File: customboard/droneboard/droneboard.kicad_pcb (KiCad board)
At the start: 4 copper layers, 38 x 38 mm, 49 parts, among them J1 Conn_01x04, J3 Conn_01x05_Pin, J4 Conn_01x02_Pin, J7 Conn_01x04_Odd_Even, SW1 SW_Push, SW2 SW_Push, U1 STM32F411CEUx, U3 L78M05CDT, U4 ICM-42688-P, U5 LDK130M33R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

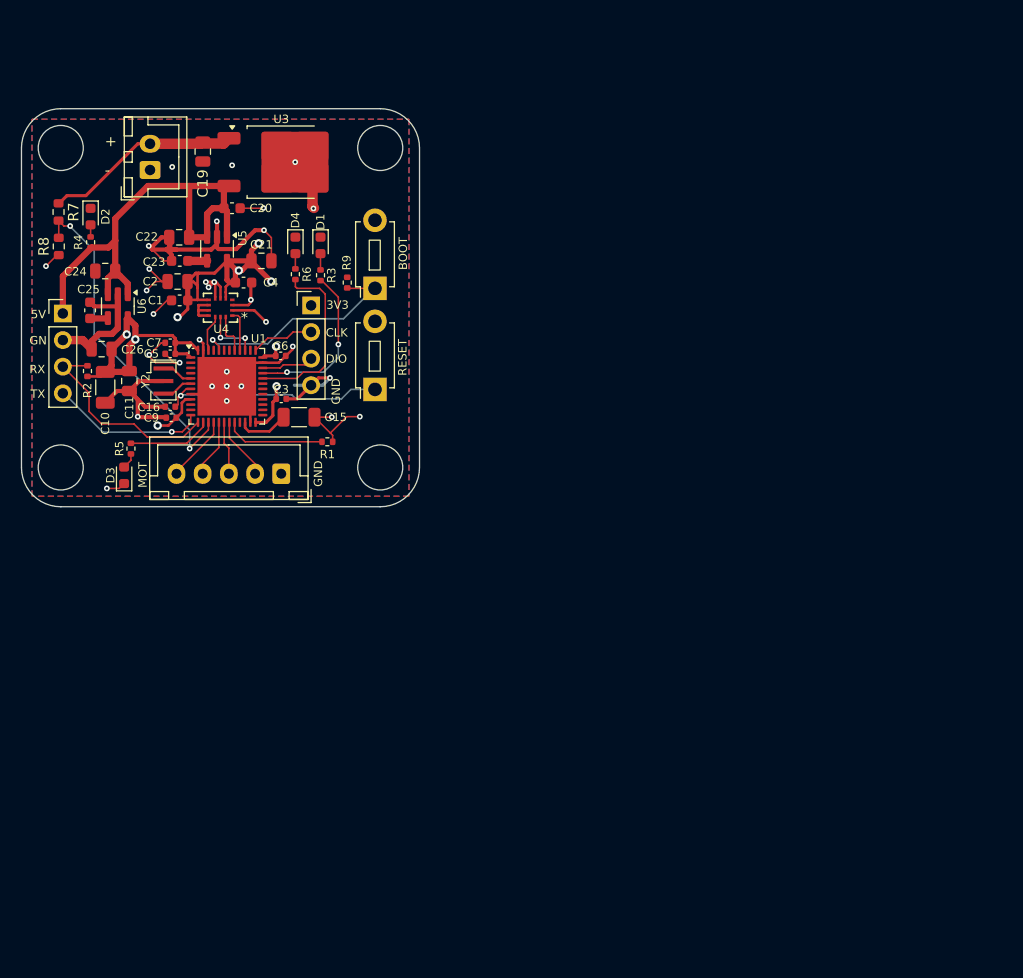
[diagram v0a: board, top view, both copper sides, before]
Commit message: stm32f7 initial work
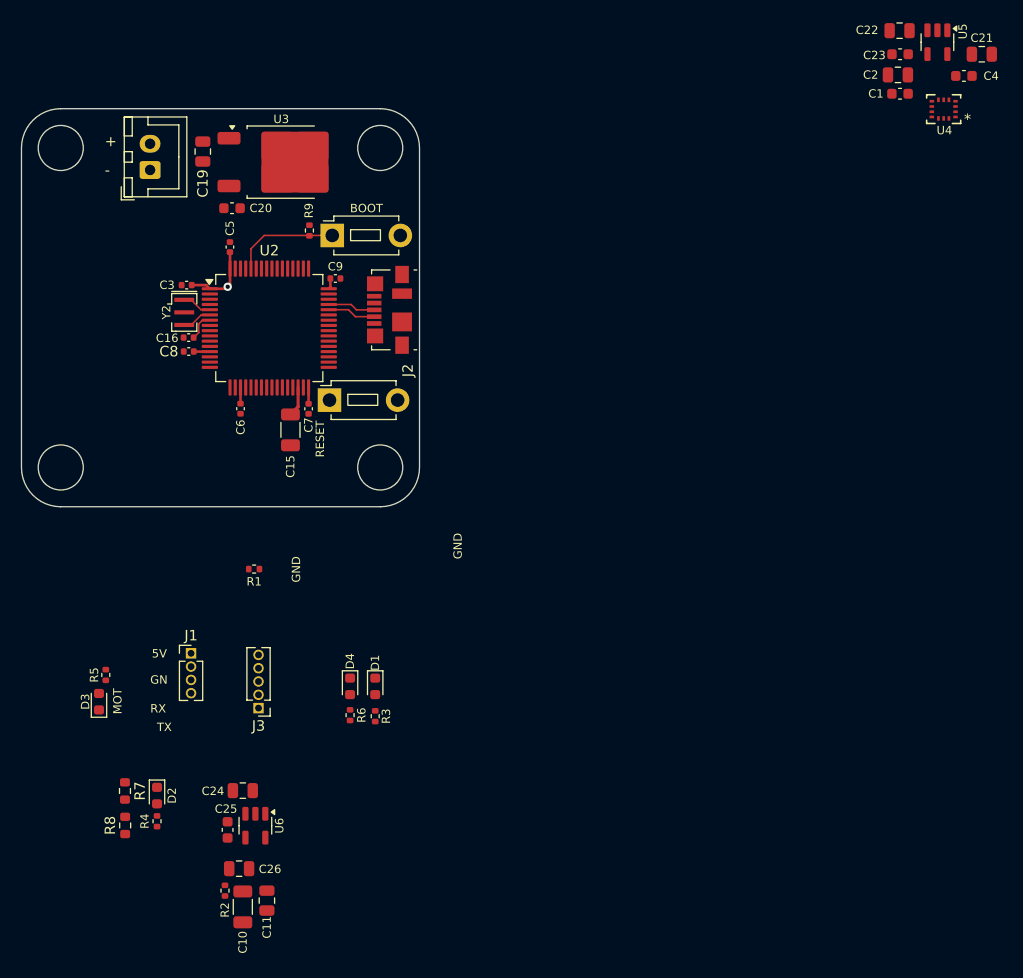
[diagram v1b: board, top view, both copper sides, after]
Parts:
- removed J7: Conn_01x04_Odd_Even, Connector_PinHeader_2.54mm:PinHeader_1x04_P2.54mm_Vertical
- removed U1: STM32F411CEUx, Package_DFN_QFN:QFN-48-1EP_7x7mm_P0.5mm_EP5.6x5.6mm
- added C8: 100n, Capacitor_SMD:C_0402_1005Metric, F.Cu at (66.0, 105.2)
- added J2: USB_B_Micro, Connector_USB:USB_Micro-B_Molex_47346-0001, F.Cu at (85.1, 101.2)
- added U2: STM32F722RETx, Package_QFP:LQFP-64_10x10mm_P0.5mm, F.Cu at (73.7, 102.9)
- J1: footprint Connector_PinHeader_2.54mm:PinHeader_1x04_P2.54mm_Vertical -> Connector_PinHeader_1.27mm:PinHeader_1x04_P1.27mm_Vertical
- J3: footprint Connector_JST:JST_XH_B5B-XH-A_1x05_P2.50mm_Vertical -> Connector_PinHeader_1.27mm:PinHeader_1x05_P1.27mm_Vertical
- moved U4 71.6 mm to (138.0, 82.0)
- moved C1 71.5 mm to (133.9, 80.6)
- moved C2 71.5 mm to (133.7, 78.8)
- moved C21 71.5 mm to (141.7, 76.8)
- moved C22 71.5 mm to (133.8, 74.5)
- moved C23 71.5 mm to (133.9, 76.8)
- moved U5 71.5 mm to (137.4, 75.6)
- moved C4 71.5 mm to (140.0, 78.9)
- moved R4 55.6 mm to (62.9, 150.0)
- moved R8 55.6 mm to (59.9, 150.4)
- moved D2 55.6 mm to (62.9, 147.6)
- moved R7 55.6 mm to (59.9, 147.1)
- moved C26 51.3 mm to (70.8, 154.6)
- moved R2 51.3 mm to (69.4, 156.7)
- moved C10 51.3 mm to (71.1, 158.2)
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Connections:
- R1 pad 1: Net-(U1-PB2) -> unconnected-(R1-Pad1)
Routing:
- net /GND: track 134.7 -> 0.00 mm, vias 31 -> 0
- net /5V: track 48.2 -> 0.00 mm
- net /VBATMON: track 32.2 -> 0.00 mm, vias 2 -> 0
- net /VGYRO: track 30.2 -> 0.00 mm, vias 4 -> 0
- net /VMCU: track 36.8 -> 12.8 mm, vias 5 -> 1
- net /RX3: track 20.0 -> 0.00 mm
- net /RESET1: track 21.9 -> 2.71 mm, vias 1 -> 0
- net /12V: track 18.9 -> 0.00 mm
- net /BLUE: track 17.1 -> 0.00 mm
- net /YELLOW: track 16.0 -> 0.00 mm, vias 2 -> 0
- net /TX3: track 14.9 -> 0.00 mm, vias 1 -> 0
- net /BOOT: track 21.8 -> 10.2 mm, vias 1 -> 0
- net Net-(U1-PB2): track 9.62 -> 0.00 mm
- net /GREEN: track 7.99 -> 0.00 mm
- net /MOTOR3: track 6.38 -> 0.00 mm
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- removed copper zone on B.Cu, net /GND
- removed copper zone on F.Cu, net /GND
- removed copper zone on In1.Cu, net /GND
- removed copper zone on In2.Cu, net /VGYRO
- removed copper zone on In2.Cu, net /VMCU
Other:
- board text removed: "3V3"
- board text removed: "CLK"
- board text removed: "DIO"
